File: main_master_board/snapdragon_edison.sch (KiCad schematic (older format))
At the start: 49 parts, among them J2 JD2-0011NL, U17 J1, U18 J2, U19 LAN9512, U21 MIC2026, U24 AS1360, U25 Si1900DL, U26 SN74LV4T125, U27 SN74LV4T125, U28 SN74LV1T125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

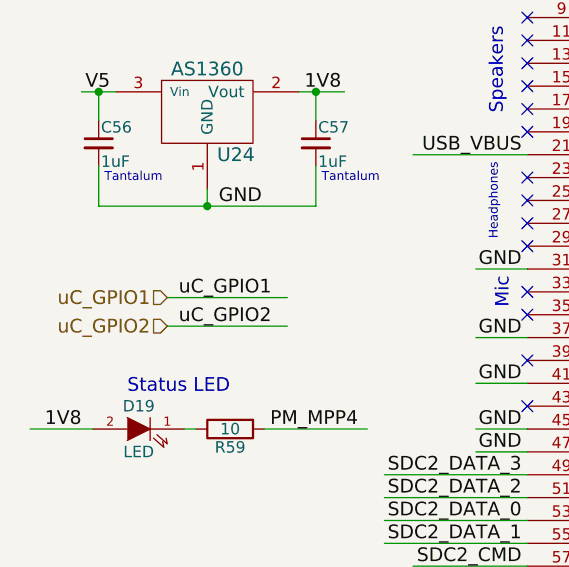
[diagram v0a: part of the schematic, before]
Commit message: Working on routing near n-p mosfets. save point incase new apporach doesn't work out
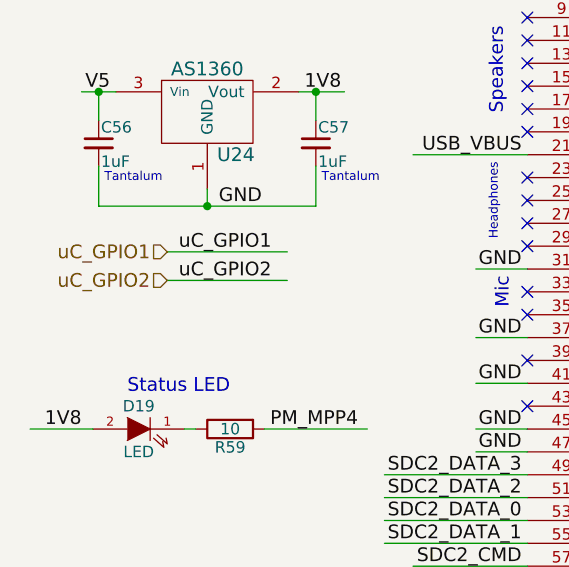
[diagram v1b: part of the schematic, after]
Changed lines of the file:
@@
 LIBS:Sensors
 LIBS:LP3852-3.3
-LIBS:0s102011ma1qn1
-LIBS:74LVC1G17
-LIBS:74V1T126
-LIBS:acs711klctr-12ab-t
-LIBS:AD7192
-LIBS:AD7193
-LIBS:am-hrr30-xxx
-LIBS:aon7528
-LIBS:AP7363
-LIBS:AS1359
-LIBS:csd16323q3
-LIBS:dmn2004dmk
-LIBS:dp_devices
-LIBS:DSPIC33E128MC506
-LIBS:fds6898az
-LIBS:ina197
-LIBS:irf7329pbf
-LIBS:ld1117
-LIBS:lm3478
-LIBS:lm3481
-LIBS:lt1910
-LIBS:ltc1871
-LIBS:ltc1982
-LIBS:MAG3110
-LIBS:mcp1700
-LIBS:mcp73831
-LIBS:mcsmt-g5030a1-3712
-LIBS:microchip_can
-LIBS:microclasp_hdrx2
-LIBS:microclasp_hdrx3
-LIBS:MPU-6000_MPU-6050
-LIBS:MPU-9150
-LIBS:nrf24l01+
-LIBS:pds1040l
-LIBS:pic12f1571
-LIBS:pinhead
-LIBS:psmn013-80ys
-LIBS:RESISTOR_ARRAY
-LIBS:rf803d
-LIBS:RGB_LED
-LIBS:Si1970DH
-LIBS:sn65hvd232
-LIBS:ssc54
-LIBS:sw_push_4
-LIBS:tc74
-LIBS:TPS2113A
-LIBS:tps54540
-LIBS:vs-mbrb1635pbf
-LIBS:xal5050-562meb
-LIBS:xal6030-182mec
+LIBS:decaWave
 LIBS:conn_2x50
 LIBS:conn_open_q_x2
@@
 LIBS:ac-dc
 LIBS:actel
+LIBS:allegro
 LIBS:Altera
 LIBS:analog_devices
@@
 LIBS:logo
 LIBS:maxim
+LIBS:mechanical
 LIBS:microchip_dspic33dsc
 LIBS:microchip_pic10mcu
@@
 LIBS:microchip_pic32mcu
 LIBS:motor_drivers
+LIBS:motors
 LIBS:msp430
 LIBS:nordicsemi
@@
 LIBS:ttl_ieee
 LIBS:video
+LIBS:wiznet
 LIBS:Worldsemi
 LIBS:Xicor
+LIBS:zetex
 LIBS:Zilog
 LIBS:conn_2x45
@@
 GND
 $Comp
-L +3.3VA #PWR019
+L +3.3VA #PWR022
 U 1 1 58837660
 P 3025 5775
-F 0 "#PWR019" H 3025 5625 50  0001 C CNN
+F 0 "#PWR022" H 3025 5625 50  0001 C CNN
 F 1 "+3.3VA" H 3025 5915 50  0000 C CNN
 F 2 "" H 3025 5775 50  0000 C CNN
@@
 GND
 $Comp
-L +1V8 #PWR020
+L +1V8 #PWR023
 U 1 1 5884251A
 P 875 7125
-F 0 "#PWR020" H 875 6975 50  0001 C CNN
+F 0 "#PWR023" H 875 6975 50  0001 C CNN
 F 1 "+1V8" H 875 7265 50  0000 C CNN
 F 2 "" H 875 7125 50  0000 C CNN
@@
 3V3
 $Comp
-L +3.3VA #PWR021
+L +3.3VA #PWR024
 U 1 1 5884804C
 P 7725 5500
-F 0 "#PWR021" H 7725 5350 50  0001 C CNN
+F 0 "#PWR024" H 7725 5350 50  0001 C CNN
 F 1 "+3.3VA" H 7725 5640 50  0000 C CNN
 F 2 "" H 7725 5500 50  0000 C CNN
@@
 $EndComp
 $Comp
-L +1V8 #PWR022
+L +1V8 #PWR025
 U 1 1 58849901
 P 4400 6225
-F 0 "#PWR022" H 4400 6075 50  0001 C CNN
+F 0 "#PWR025" H 4400 6075 50  0001 C CNN
 F 1 "+1V8" H 4400 6365 50  0000 C CNN
 F 2 "" H 4400 6225 50  0000 C CNN
@@
 $EndComp
 $Comp
-L +3.3VA #PWR023
+L +3.3VA #PWR026
 U 1 1 5885B0EB
 P 10325 8100
-F 0 "#PWR023" H 10325 7950 50  0001 C CNN
+F 0 "#PWR026" H 10325 7950 50  0001 C CNN
 F 1 "+3.3VA" H 10325 8240 50  0000 C CNN
 F 2 "" H 10325 8100 50  0000 C CNN
@@
 Text Label 14050 2050 0    60   ~ 0
 UART1_TX_3V3
-Text HLabel 1175 2425 0    60   Input ~ 0
+Text HLabel 1175 2225 0    60   Input ~ 0
 uC_GPIO1
-Text HLabel 1175 2550 0    60   Input ~ 0
+Text HLabel 1175 2350 0    60   Input ~ 0
 uC_GPIO2
-Text Label 1225 2425 0    60   ~ 0
+Text Label 1225 2225 0    60   ~ 0
 uC_GPIO1
-Text Label 1225 2550 0    60   ~ 0
+Text Label 1225 2350 0    60   ~ 0
 uC_GPIO2
 Text Label 9875 3100 0    60   ~ 0
@@
 Connection ~ 9900 1525
 Wire Wire Line
-	1175 2425 1700 2425
-Wire Wire Line
-	1175 2550 1700 2550
+	1175 2225 1700 2225
+Wire Wire Line
+	1175 2350 1700 2350
 Wire Wire Line
 	9825 3100 10350 3100

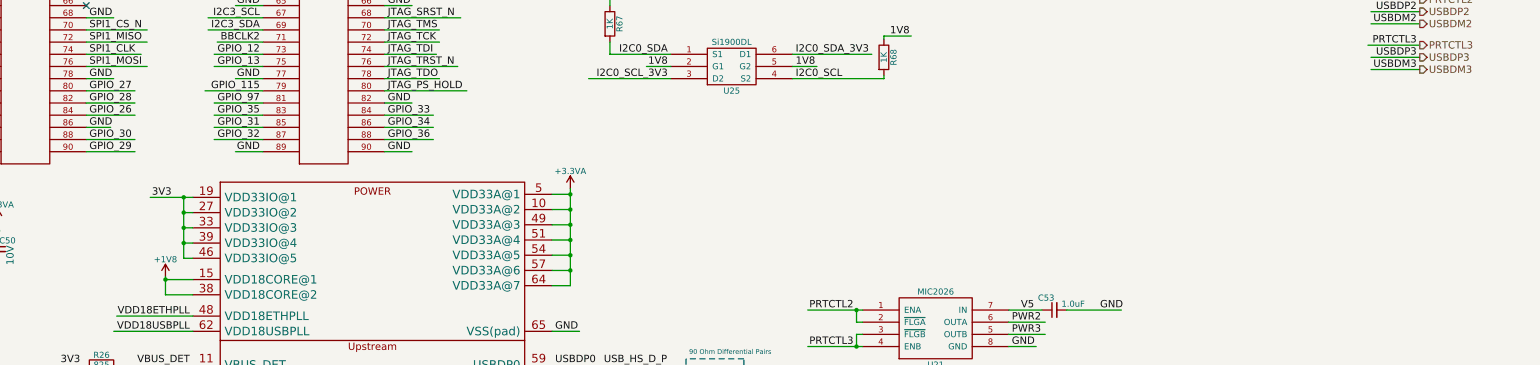
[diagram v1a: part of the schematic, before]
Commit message: Changed expansion connector to two connectors. Routed 5 to 4 buck.
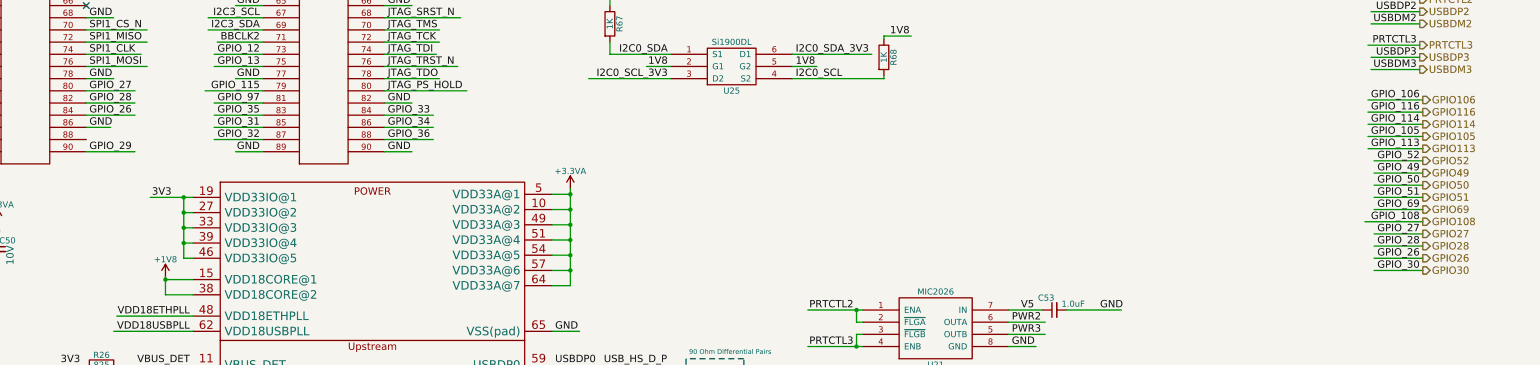
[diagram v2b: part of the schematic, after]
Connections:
- net labels added: GPIO105, GPIO106, GPIO108, GPIO113, GPIO114, GPIO116, GPIO26, GPIO27, GPIO28, GPIO30, GPIO49, GPIO50, GPIO51, GPIO52, GPIO69
- wire segments 379 -> 393
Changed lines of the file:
@@
 Text Label 3775 5200 0    60   ~ 0
 GPIO_29
-Text Label 3775 5100 0    60   ~ 0
+Text Label 14700 6175 2    60   ~ 0
 GPIO_30
 Text Label 3775 4900 0    60   ~ 0
@@
 GND
 $Comp
-L +3.3VA #PWR022
+L +3.3VA #PWR025
 U 1 1 58837660
 P 3025 5775
-F 0 "#PWR022" H 3025 5625 50  0001 C CNN
+F 0 "#PWR025" H 3025 5625 50  0001 C CNN
 F 1 "+3.3VA" H 3025 5915 50  0000 C CNN
 F 2 "" H 3025 5775 50  0000 C CNN
@@
 GND
 $Comp
-L +1V8 #PWR023
+L +1V8 #PWR026
 U 1 1 5884251A
 P 875 7125
-F 0 "#PWR023" H 875 6975 50  0001 C CNN
+F 0 "#PWR026" H 875 6975 50  0001 C CNN
 F 1 "+1V8" H 875 7265 50  0000 C CNN
 F 2 "" H 875 7125 50  0000 C CNN
@@
 3V3
 $Comp
-L +3.3VA #PWR024
+L +3.3VA #PWR027
 U 1 1 5884804C
 P 7725 5500
-F 0 "#PWR024" H 7725 5350 50  0001 C CNN
+F 0 "#PWR027" H 7725 5350 50  0001 C CNN
 F 1 "+3.3VA" H 7725 5640 50  0000 C CNN
 F 2 "" H 7725 5500 50  0000 C CNN
@@
 $EndComp
 $Comp
-L +1V8 #PWR025
+L +1V8 #PWR028
 U 1 1 58849901
 P 4400 6225
-F 0 "#PWR025" H 4400 6075 50  0001 C CNN
+F 0 "#PWR028" H 4400 6075 50  0001 C CNN
 F 1 "+1V8" H 4400 6365 50  0000 C CNN
 F 2 "" H 4400 6225 50  0000 C CNN
@@
 $EndComp
 $Comp
-L +3.3VA #PWR026
+L +3.3VA #PWR029
 U 1 1 5885B0EB
 P 10325 8100
-F 0 "#PWR026" H 10325 7950 50  0001 C CNN
+F 0 "#PWR029" H 10325 7950 50  0001 C CNN
 F 1 "+3.3VA" H 10325 8240 50  0000 C CNN
 F 2 "" H 10325 8100 50  0000 C CNN
@@
 	3750 4900 4150 4900
 Wire Wire Line
-	3750 5100 4150 5100
+	14725 6175 14325 6175
 Wire Wire Line
 	3750 5200 4150 5200
@@
 Wire Wire Line
 	14700 4525 14300 4525
+Text HLabel 14725 4775 2    60   Output ~ 0
+GPIO106
+Text HLabel 14725 4875 2    60   Output ~ 0
+GPIO116
+Text HLabel 14725 5075 2    60   Output ~ 0
+GPIO105
+Text HLabel 14725 4975 2    60   Output ~ 0
+GPIO114
+Text HLabel 14725 5175 2    60   Output ~ 0
+GPIO113
+Text HLabel 14725 5275 2    60   Output ~ 0
+GPIO52
+Text HLabel 14725 5375 2    60   Output ~ 0
+GPIO49
+Text HLabel 14725 5575 2    60   Output ~ 0
+GPIO51
+Text HLabel 14725 5475 2    60   Output ~ 0
+GPIO50
+Text HLabel 14725 5675 2    60   Output ~ 0
+GPIO69
+Text HLabel 14725 5775 2    60   Output ~ 0
+GPIO108
+Text HLabel 14725 5875 2    60   Output ~ 0
+GPIO27
+Text HLabel 14725 6075 2    60   Output ~ 0
+GPIO26
+Text HLabel 14725 5975 2    60   Output ~ 0
+GPIO28
+Text HLabel 14725 6175 2    60   Output ~ 0
+GPIO30
+Text Label 14700 4775 2    60   ~ 0
+GPIO_106
+Text Label 14700 4875 2    60   ~ 0
+GPIO_116
+Text Label 14700 4975 2    60   ~ 0
+GPIO_114
+Text Label 14700 5075 2    60   ~ 0
+GPIO_105
+Text Label 14700 5175 2    60   ~ 0
+GPIO_113
+Wire Wire Line
+	14725 4775 14275 4775
+Wire Wire Line
+	14725 4875 14275 4875
+Wire Wire Line
+	14275 4975 14725 4975
+Wire Wire Line
+	14725 5075 14275 5075
+Wire Wire Line
+	14725 5175 14275 5175
+Text Label 14700 5275 2    60   ~ 0
+GPIO_52
+Text Label 14700 5375 2    60   ~ 0
+GPIO_49
+Text Label 14700 5475 2    60   ~ 0
+GPIO_50
+Text Label 14700 5575 2    60   ~ 0
+GPIO_51
+Text Label 14700 5675 2    60   ~ 0
+GPIO_69
+Text Label 14700 5775 2    60   ~ 0
+GPIO_108
+Wire Wire Line
+	14725 5775 14250 5775
+Wire Wire Line
+	14725 5675 14325 5675
+Wire Wire Line
+	14725 5575 14325 5575
+Wire Wire Line
+	14725 5475 14325 5475
+Wire Wire Line
+	14725 5375 14325 5375
+Wire Wire Line
+	14725 5275 14325 5275
+Text Label 14700 6075 2    60   ~ 0
+GPIO_26
+Text Label 14700 5975 2    60   ~ 0
+GPIO_28
+Text Label 14700 5875 2    60   ~ 0
+GPIO_27
+Wire Wire Line
+	14725 5875 14325 5875
+Wire Wire Line
+	14725 5975 14325 5975
+Wire Wire Line
+	14725 6075 14325 6075
 $EndSCHEMATC

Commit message: Added antenna for DART board. Also fixed 90 pin connector placement (was 180 degrees wrong). Placed Dart Board in position.
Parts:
- added C60: 5.6pF, Capacitors_SMD:C_0402, symbol C
- added L6: 2.2nH, Resistors_SMD:R_0402, symbol L
- added L7: 3.3nH, Resistors_SMD:R_0402, symbol L
- added U23: Antenna, antenna:FR05-S1-NO-104B, symbol Antenna
- added U33: conn_smt, antenna:U.FL-R-SMT-1(01), symbol conn_smt
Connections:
- net labels removed: GPIO106, GPIO116
- wire segments 393 -> 401
- no-connect marks 66 -> 67
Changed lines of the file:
@@
 LIBS:Sensors
 LIBS:LP3852-3.3
-LIBS:decaWave
+LIBS:0s102011ma1qn1
+LIBS:74LVC1G17
+LIBS:74V1T126
+LIBS:acs711klctr-12ab-t
+LIBS:AD7192
+LIBS:AD7193
+LIBS:am-hrr30-xxx
+LIBS:aon7528
+LIBS:AP7363
+LIBS:AS1359
+LIBS:csd16323q3
+LIBS:dmn2004dmk
+LIBS:dp_devices
+LIBS:DSPIC33E128MC506
+LIBS:fds6898az
+LIBS:ina197
+LIBS:irf7329pbf
+LIBS:ld1117
+LIBS:lm3478
+LIBS:lm3481
+LIBS:lt1910
+LIBS:ltc1871
+LIBS:ltc1982
+LIBS:MAG3110
+LIBS:mcp1700
+LIBS:mcp73831
+LIBS:mcsmt-g5030a1-3712
+LIBS:microchip_can
+LIBS:microclasp_hdrx2
+LIBS:microclasp_hdrx3
+LIBS:MPU-6000_MPU-6050
+LIBS:MPU-9150
+LIBS:nrf24l01+
+LIBS:pds1040l
+LIBS:pic12f1571
+LIBS:pinhead
+LIBS:psmn013-80ys
+LIBS:RESISTOR_ARRAY
+LIBS:rf803d
+LIBS:RGB_LED
+LIBS:Si1970DH
+LIBS:sn65hvd232
+LIBS:ssc54
+LIBS:sw_push_4
+LIBS:tc74
+LIBS:TPS2113A
+LIBS:tps54540
+LIBS:vs-mbrb1635pbf
+LIBS:xal5050-562meb
+LIBS:xal6030-182mec
 LIBS:conn_2x50
 LIBS:conn_open_q_x2
@@
 LIBS:ac-dc
 LIBS:actel
-LIBS:allegro
 LIBS:Altera
 LIBS:analog_devices
@@
 LIBS:logo
 LIBS:maxim
-LIBS:mechanical
 LIBS:microchip_dspic33dsc
 LIBS:microchip_pic10mcu
@@
 LIBS:microchip_pic32mcu
 LIBS:motor_drivers
-LIBS:motors
 LIBS:msp430
 LIBS:nordicsemi
@@
 LIBS:ttl_ieee
 LIBS:video
-LIBS:wiznet
 LIBS:Worldsemi
 LIBS:Xicor
-LIBS:zetex
 LIBS:Zilog
 LIBS:conn_2x45
@@
 LIBS:Si1077X
 LIBS:LTC2955-1
+LIBS:antenna
 LIBS:main_master_board-cache
 EELAYER 25 0
@@
 GND
 $Comp
-L +3.3VA #PWR025
+L +3.3VA #PWR26
 U 1 1 58837660
 P 3025 5775
-F 0 "#PWR025" H 3025 5625 50  0001 C CNN
+F 0 "#PWR26" H 3025 5625 50  0001 C CNN
 F 1 "+3.3VA" H 3025 5915 50  0000 C CNN
 F 2 "" H 3025 5775 50  0000 C CNN
@@
 GND
 $Comp
-L +1V8 #PWR026
+L +1V8 #PWR25
 U 1 1 5884251A
 P 875 7125
-F 0 "#PWR026" H 875 6975 50  0001 C CNN
+F 0 "#PWR25" H 875 6975 50  0001 C CNN
 F 1 "+1V8" H 875 7265 50  0000 C CNN
 F 2 "" H 875 7125 50  0000 C CNN
@@
 3V3
 $Comp
-L +3.3VA #PWR027
+L +3.3VA #PWR28
 U 1 1 5884804C
 P 7725 5500
-F 0 "#PWR027" H 7725 5350 50  0001 C CNN
+F 0 "#PWR28" H 7725 5350 50  0001 C CNN
 F 1 "+3.3VA" H 7725 5640 50  0000 C CNN
 F 2 "" H 7725 5500 50  0000 C CNN
@@
 $EndComp
 $Comp
-L +1V8 #PWR028
+L +1V8 #PWR27
 U 1 1 58849901
 P 4400 6225
-F 0 "#PWR028" H 4400 6075 50  0001 C CNN
+F 0 "#PWR27" H 4400 6075 50  0001 C CNN
 F 1 "+1V8" H 4400 6365 50  0000 C CNN
 F 2 "" H 4400 6225 50  0000 C CNN
@@
 $EndComp
 $Comp
-L +3.3VA #PWR029
+L +3.3VA #PWR29
 U 1 1 5885B0EB
 P 10325 8100
-F 0 "#PWR029" H 10325 7950 50  0001 C CNN
+F 0 "#PWR29" H 10325 7950 50  0001 C CNN
 F 1 "+3.3VA" H 10325 8240 50  0000 C CNN
 F 2 "" H 10325 8100 50  0000 C CNN
@@
 Wire Wire Line
 	1600 3000 2050 3000
-Text Label 14675 3950 2    60   ~ 0
-PRTCTL2
 Text Label 14675 4050 2    60   ~ 0
 USBDP2
 Text Label 14675 4150 2    60   ~ 0
 USBDM2
-Text Label 14675 4325 2    60   ~ 0
-PRTCTL3
 Text Label 14675 4425 2    60   ~ 0
 USBDP3
@@
 SDC2_DATA_1
 Text HLabel 14700 3950 2    60   Output ~ 0
-PRTCTL2
+PWR2
 Text HLabel 14700 4050 2    60   Output ~ 0
 USBDP2
@@
 USBDM2
 Text HLabel 14700 4325 2    60   Output ~ 0
-PRTCTL3
+PWR3
 Text HLabel 14700 4425 2    60   Output ~ 0
 USBDP3
@@
 Wire Wire Line
 	14700 4525 14300 4525
-Text HLabel 14725 4775 2    60   Output ~ 0
-GPIO106
-Text HLabel 14725 4875 2    60   Output ~ 0
-GPIO116
 Text HLabel 14725 5075 2    60   Output ~ 0
 GPIO105
@@
 Text HLabel 14725 6175 2    60   Output ~ 0
 GPIO30
-Text Label 14700 4775 2    60   ~ 0
-GPIO_106
-Text Label 14700 4875 2    60   ~ 0
-GPIO_116
 Text Label 14700 4975 2    60   ~ 0
 GPIO_114
@@
 Text Label 14700 5175 2    60   ~ 0
 GPIO_113
-Wire Wire Line
-	14725 4775 14275 4775
-Wire Wire Line
-	14725 4875 14275 4875
 Wire Wire Line
 	14275 4975 14725 4975
@@
 Wire Wire Line
 	14725 6075 14325 6075
+Text Label 14675 4325 2    60   ~ 0
+PWR3
+Text Label 14675 3950 2    60   ~ 0
+PWR2
+$Comp
+L Antenna U23
+U 1 1 58995623
+P 13975 8100
+F 0 "U23" H 13975 7975 60  0000 C CNN
+F 1 "Antenna" H 13975 8225 60  0000 C CNN
+F 2 "antenna:FR05-S1-NO-104B" H 13975 8100 60  0001 C CNN
+F 3 "http://www.richardsonrfpd.com/pages/Product-Details.aspx?productId=921210" H 13975 8100 60  0001 C CNN
+	1    13975 8100
+	1    0    0    -1
+$EndComp
+$Comp
+L L L6
+U 1 1 58995B96
+P 14450 8325
+F 0 "L6" V 14400 8325 50  0000 C CNN
+F 1 "2.2nH" V 14525 8325 50  0000 C CNN
+F 2 "Resistors_SMD:R_0402" H 14450 8325 50  0001 C CNN
+F 3 "" H 14450 8325 50  0000 C CNN
+F 4 "400mA" V 14600 8325 60  0000 C CNN "Amps"
+	1    14450 8325
+	1    0    0    -1
+$EndComp
+$Comp
+L C C60
+U 1 1 58995C8C
+P 14750 8100
+F 0 "C60" V 14800 8200 50  0000 L CNN
+F 1 "5.6pF" V 14800 7850 50  0000 L CNN
+F 2 "Capacitors_SMD:C_0402" H 14788 7950 50  0001 C CNN
+F 3 "" H 14750 8100 50  0000 C CNN
+	1    14750 8100
+	0    -1   -1   0
+$EndComp
+$Comp
+L L L7
+U 1 1 58995F41
+P 15025 8300
+F 0 "L7" V 14975 8300 50  0000 C CNN
+F 1 "3.3nH" V 15100 8300 50  0000 C CNN
+F 2 "Resistors_SMD:R_0402" H 15025 8300 50  0001 C CNN
+F 3 "" H 15025 8300 50  0000 C CNN
+F 4 "400mA" V 15175 8300 60  0000 C CNN "Amps"
+	1    15025 8300
+	1    0    0    -1
+$EndComp
+$Comp
+L conn_smt U33
+U 1 1 58996283
+P 15500 8100
+F 0 "U33" H 15500 7925 60  0000 C CNN
+F 1 "conn_smt" H 15500 8275 60  0000 C CNN
+F 2 "antenna:U.FL-R-SMT-1(01)" H 15500 8100 60  0001 C CNN
+F 3 "http://www.digikey.com/product-detail/en/U.FL-R-SMT-1%2801%29/H122041-ND/3978494" H 15500 8100 60  0001 C CNN
+	1    15500 8100
+	1    0    0    -1
+$EndComp
+Wire Wire Line
+	14325 8100 14600 8100
+Wire Wire Line
+	14450 8175 14450 8100
+Connection ~ 14450 8100
+Wire Wire Line
+	14900 8100 15175 8100
+Wire Wire Line
+	15025 8150 15025 8100
+Connection ~ 15025 8100
+Wire Wire Line
+	14450 8475 14450 8575
+Wire Wire Line
+	14450 8575 15875 8575
+Wire Wire Line
+	15025 8575 15025 8450
+Wire Wire Line
+	15800 8050 15875 8050
+Wire Wire Line
+	15800 8150 15875 8150
+Connection ~ 15875 8150
+NoConn ~ 13625 8100
+Connection ~ 15025 8575
+Wire Wire Line
+	15875 8050 15875 8575
+Text Label 15100 8575 0    60   ~ 0
+GND
 $EndSCHEMATC

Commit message: Stuff?
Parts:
- removed U23: Antenna, antenna:FR05-S1-NO-104B, symbol Antenna
- added U23: antenna, antenna:FR05-S1-NO-104B, symbol antenna
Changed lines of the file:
@@
 LIBS:Sensors
 LIBS:LP3852-3.3
-LIBS:0s102011ma1qn1
-LIBS:74LVC1G17
-LIBS:74V1T126
-LIBS:acs711klctr-12ab-t
-LIBS:AD7192
-LIBS:AD7193
-LIBS:am-hrr30-xxx
-LIBS:aon7528
-LIBS:AP7363
-LIBS:AS1359
-LIBS:csd16323q3
-LIBS:dmn2004dmk
-LIBS:dp_devices
-LIBS:DSPIC33E128MC506
-LIBS:fds6898az
-LIBS:ina197
-LIBS:irf7329pbf
-LIBS:ld1117
-LIBS:lm3478
-LIBS:lm3481
-LIBS:lt1910
-LIBS:ltc1871
-LIBS:ltc1982
-LIBS:MAG3110
-LIBS:mcp1700
-LIBS:mcp73831
-LIBS:mcsmt-g5030a1-3712
-LIBS:microchip_can
-LIBS:microclasp_hdrx2
-LIBS:microclasp_hdrx3
-LIBS:MPU-6000_MPU-6050
-LIBS:MPU-9150
-LIBS:nrf24l01+
-LIBS:pds1040l
-LIBS:pic12f1571
-LIBS:pinhead
-LIBS:psmn013-80ys
-LIBS:RESISTOR_ARRAY
-LIBS:rf803d
-LIBS:RGB_LED
-LIBS:Si1970DH
-LIBS:sn65hvd232
-LIBS:ssc54
-LIBS:sw_push_4
-LIBS:tc74
-LIBS:TPS2113A
-LIBS:tps54540
-LIBS:vs-mbrb1635pbf
-LIBS:xal5050-562meb
-LIBS:xal6030-182mec
+LIBS:decaWave
 LIBS:conn_2x50
 LIBS:conn_open_q_x2
@@
 LIBS:ac-dc
 LIBS:actel
+LIBS:allegro
 LIBS:Altera
 LIBS:analog_devices
@@
 LIBS:logo
 LIBS:maxim
+LIBS:mechanical
 LIBS:microchip_dspic33dsc
 LIBS:microchip_pic10mcu
@@
 LIBS:microchip_pic32mcu
 LIBS:motor_drivers
+LIBS:motors
 LIBS:msp430
 LIBS:nordicsemi
@@
 LIBS:ttl_ieee
 LIBS:video
+LIBS:wiznet
 LIBS:Worldsemi
 LIBS:Xicor
+LIBS:zetex
 LIBS:Zilog
 LIBS:conn_2x45
@@
 PWR2
 $Comp
-L Antenna U23
-U 1 1 58995623
-P 13975 8100
-F 0 "U23" H 13975 7975 60  0000 C CNN
-F 1 "Antenna" H 13975 8225 60  0000 C CNN
-F 2 "antenna:FR05-S1-NO-104B" H 13975 8100 60  0001 C CNN
-F 3 "http://www.richardsonrfpd.com/pages/Product-Details.aspx?productId=921210" H 13975 8100 60  0001 C CNN
-	1    13975 8100
-	1    0    0    -1
-$EndComp
-$Comp
 L L L6
 U 1 1 58995B96
@@
 Text Label 15100 8575 0    60   ~ 0
 GND
+$Comp
+L antenna U23
+U 1 1 58965192
+P 13975 8100
+F 0 "U23" H 13975 7975 60  0000 C CNN
+F 1 "antenna" H 13975 8225 60  0000 C CNN
+F 2 "antenna:FR05-S1-NO-104B" H 13975 8100 60  0001 C CNN
+F 3 "" H 13975 8100 60  0001 C CNN
+	1    13975 8100
+	1    0    0    -1
+$EndComp
 $EndSCHEMATC

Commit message: Started differential routing for USB and Ethernet.
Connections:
- net labels added: RX_N, RX_P, TX_N, TX_P, USBDM2_N, USBDM3_N, USBDP2_P, USBDP3_P, USBPM3_N, USB_HS_D_N
- net labels removed: RXN, RXP, TXN, TXP, USBDM0, USBDP0, USBPM3, USB_HS_D_M
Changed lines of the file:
@@
 GPIO_20
 Text Label 6225 2300 0    60   ~ 0
-USB_HS_D_M
+USB_HS_D_N
 Text Label 6225 2400 0    60   ~ 0
 USB_HS_D_P
@@
 GND
 $Comp
-L +3.3VA #PWR26
+L +3.3VA #PWR025
 U 1 1 58837660
 P 3025 5775
-F 0 "#PWR26" H 3025 5625 50  0001 C CNN
+F 0 "#PWR025" H 3025 5625 50  0001 C CNN
 F 1 "+3.3VA" H 3025 5915 50  0000 C CNN
 F 2 "" H 3025 5775 50  0000 C CNN
@@
 GND
 $Comp
-L +1V8 #PWR25
+L +1V8 #PWR026
 U 1 1 5884251A
 P 875 7125
-F 0 "#PWR25" H 875 6975 50  0001 C CNN
+F 0 "#PWR026" H 875 6975 50  0001 C CNN
 F 1 "+1V8" H 875 7265 50  0000 C CNN
 F 2 "" H 875 7125 50  0000 C CNN
@@
 3V3
 $Comp
-L +3.3VA #PWR28
+L +3.3VA #PWR027
 U 1 1 5884804C
 P 7725 5500
-F 0 "#PWR28" H 7725 5350 50  0001 C CNN
+F 0 "#PWR027" H 7725 5350 50  0001 C CNN
 F 1 "+3.3VA" H 7725 5640 50  0000 C CNN
 F 2 "" H 7725 5500 50  0000 C CNN
@@
 $EndComp
 $Comp
-L +1V8 #PWR27
+L +1V8 #PWR028
 U 1 1 58849901
 P 4400 6225
-F 0 "#PWR27" H 4400 6075 50  0001 C CNN
+F 0 "#PWR028" H 4400 6075 50  0001 C CNN
 F 1 "+1V8" H 4400 6365 50  0000 C CNN
 F 2 "" H 4400 6225 50  0000 C CNN
@@
 Text Label 4600 7475 2    60   ~ 0
 PRTCTL3
-Text Label 7600 6950 0    60   ~ 0
-USBDP0
-Text Label 7600 7075 0    60   ~ 0
-USBDM0
 Text Label 7600 7350 0    60   ~ 0
-USBDP2
+USBDP2_P
 Text Label 7600 7475 0    60   ~ 0
-USBDM2
+USBDM2_N
 Text Label 7600 7650 0    60   ~ 0
-USBDP3
+USBDP3_P
 Text Label 7600 7775 0    60   ~ 0
-USBPM3
+USBPM3_N
 $Comp
 L R R30
@@
 3V3
 Text Label 7600 8475 0    60   ~ 0
-RXP
+RX_P
 Text Label 7600 8575 0    60   ~ 0
-RXN
+RX_N
 Text Label 7600 8725 0    60   ~ 0
-TXP
+TX_P
 Text Label 7600 8825 0    60   ~ 0
-TXN
+TX_N
 NoConn ~ 4625 9100
 NoConn ~ 4625 9475
@@
 Text Label 3700 6950 2    60   ~ 0
 3V3
-Text Label 8000 7075 0    60   ~ 0
-USB_HS_D_M
-Text Label 8000 6950 0    60   ~ 0
+Text Label 7600 7075 0    60   ~ 0
+USB_HS_D_N
+Text Label 7600 6950 0    60   ~ 0
 USB_HS_D_P
 NoConn ~ 10850 9150
@@
 $EndComp
 $Comp
-L +3.3VA #PWR29
+L +3.3VA #PWR029
 U 1 1 5885B0EB
 P 10325 8100
-F 0 "#PWR29" H 10325 7950 50  0001 C CNN
+F 0 "#PWR029" H 10325 7950 50  0001 C CNN
 F 1 "+3.3VA" H 10325 8240 50  0000 C CNN
 F 2 "" H 10325 8100 50  0000 C CNN
@@
 Text Notes 10025 8250 0    39   ~ 0
 place near lan9512
-Text Label 10700 8550 0    60   ~ 0
-TXP
-Text Label 10700 8650 0    60   ~ 0
-TXN
-Text Label 10700 8750 0    60   ~ 0
-RXP
-Text Label 10700 9050 0    60   ~ 0
-RXN
+Text Label 10675 8750 0    60   ~ 0
+RX_P
+Text Label 10675 9050 0    60   ~ 0
+RX_N
 Text Label 10825 9250 2    60   ~ 0
 GND
@@
 Text Label 1400 2025 0    60   ~ 0
 GND
-Text Label 925  1525 2    60   ~ 0
-V5
 Text Label 1775 1525 0    60   ~ 0
 1V8
@@
 	1600 3000 2050 3000
 Text Label 14675 4050 2    60   ~ 0
-USBDP2
+USBDP2_P
 Text Label 14675 4150 2    60   ~ 0
-USBDM2
+USBDM2_N
 Text Label 14675 4425 2    60   ~ 0
-USBDP3
+USBDP3_P
 Text Label 14675 4525 2    60   ~ 0
-USBDM3
+USBDM3_N
 Text Label 14675 2875 2    60   ~ 0
 I2C1_SCL
@@
 	1    0    0    -1
 $EndComp
+Text Label 825  1525 0    60   ~ 0
+V4
+Text Label 10675 8550 0    60   ~ 0
+TX_P
+Text Label 10675 8650 0    60   ~ 0
+TX_N
 $EndSCHEMATC
